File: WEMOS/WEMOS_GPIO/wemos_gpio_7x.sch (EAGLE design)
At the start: 24 parts

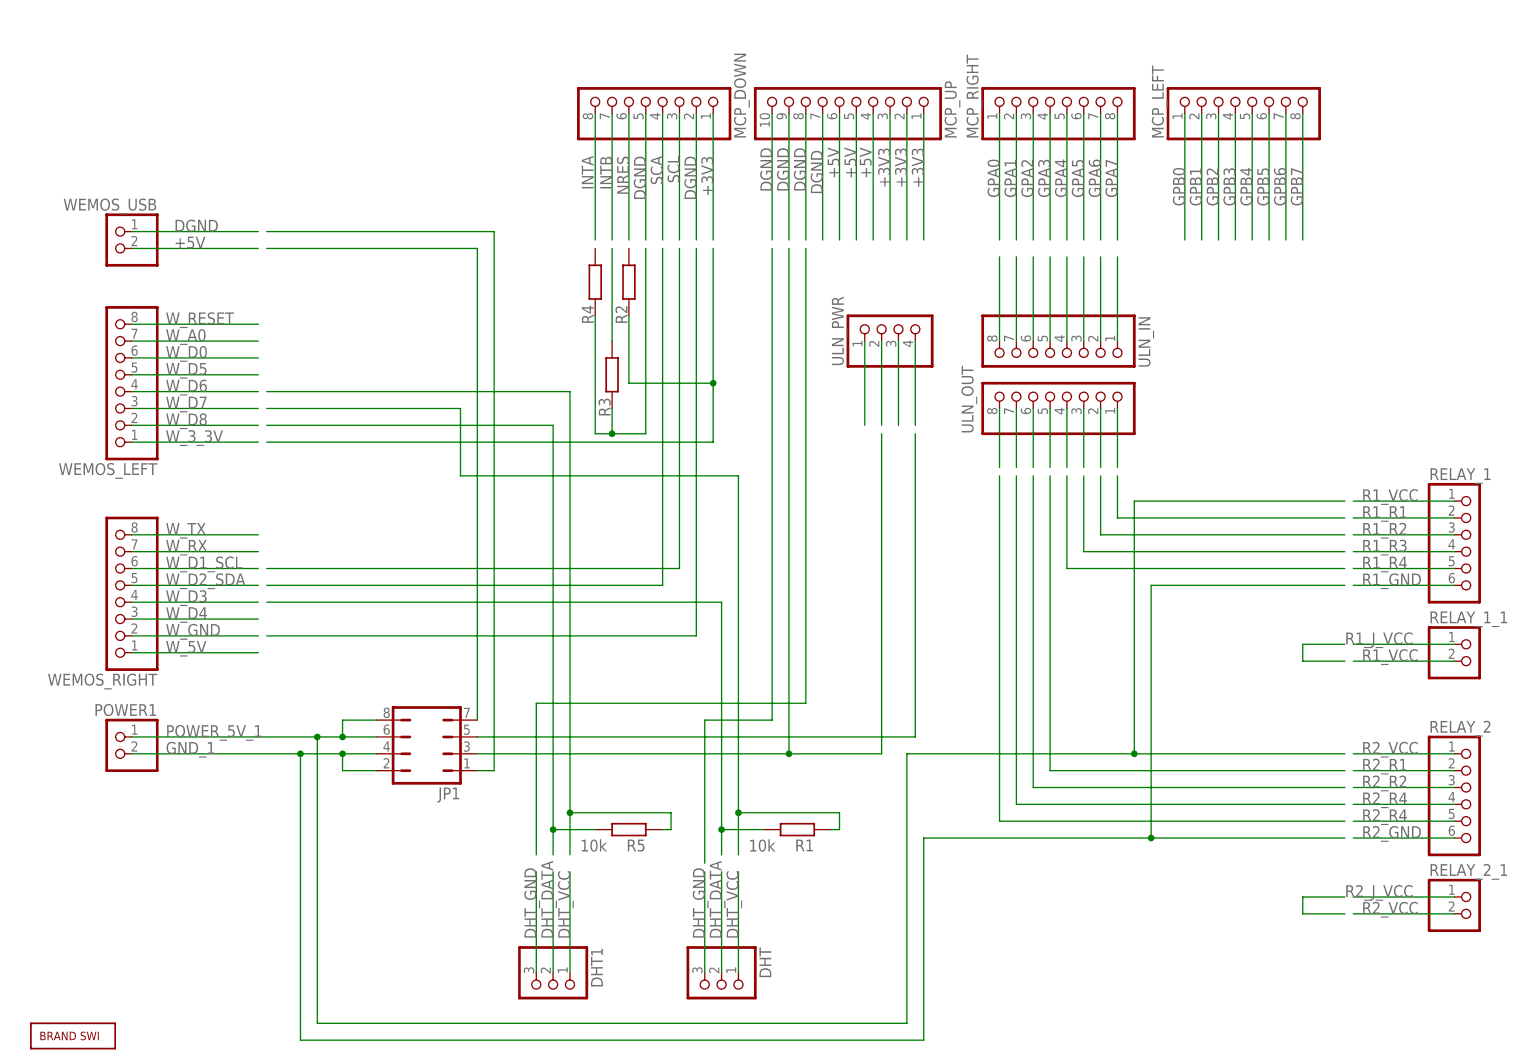
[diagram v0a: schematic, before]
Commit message: reworked wemos gpio, reworked wiring for garden control
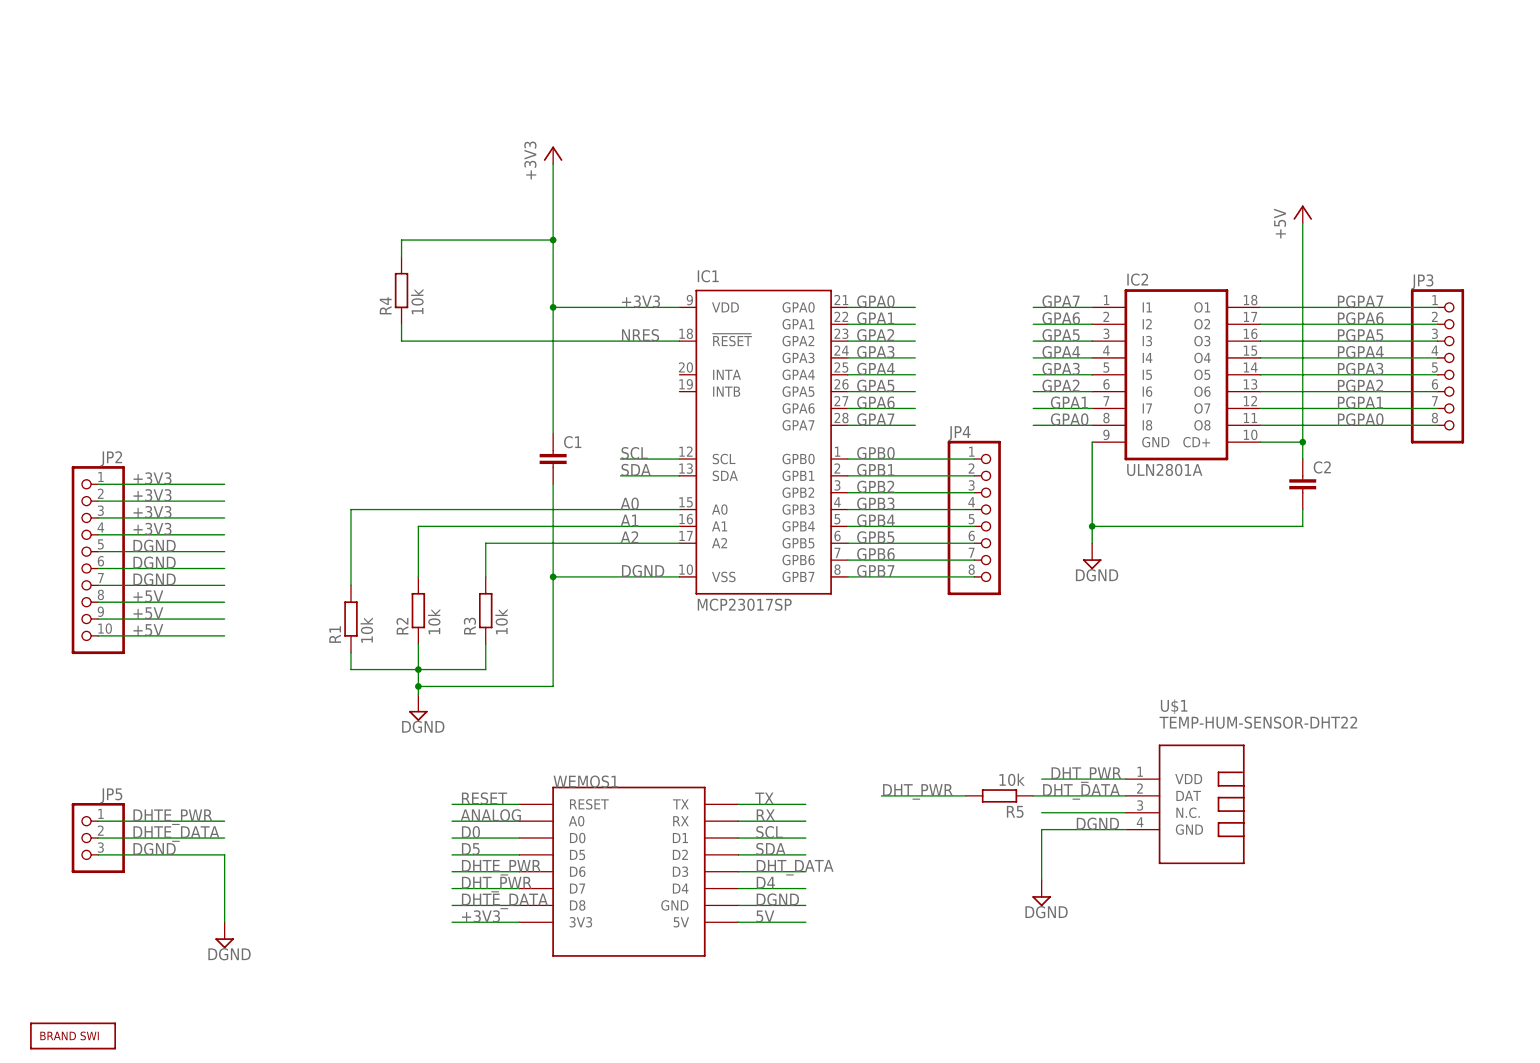
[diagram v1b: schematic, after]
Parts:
- removed DHT, DHT1: (no value), pinhead:PINHD-1X3
- removed JP1: (no value), jumper:JP4Q
- removed MCP_DOWN, MCP_LEFT, MCP_RIGHT, ULN_IN, ULN_OUT, WEMOS_LEFT, WEMOS_RIGHT: (no value), pinhead:PINHD-1X8
- removed MCP_UP: (no value), pinhead:PINHD-1X10
- removed POWER1, RELAY_1_1, RELAY_2_1, WEMOS_USB: (no value), pinhead:PINHD-1X2
- removed RELAY_1, RELAY_2: (no value), pinhead:PINHD-1X6
- removed ULN_PWR: (no value), pinhead:PINHD-1X4
- added C1, C2: (no value), rcl:C-EUC1210
- added IC1: MCP23017SP, SWI_COMMONS:MCP23017SP
- added IC2: ULN2801A, uln-udn:ULN2801A
- added JP2: (no value), pinhead:PINHD-1X10
- added JP3, JP4: (no value), pinhead:PINHD-1X8
- added JP5: (no value), pinhead:PINHD-1X3
- added U$1: TEMP-HUM-SENSOR-DHT22, SWI_COMMONS:TEMP-HUM-SENSOR-DHT22
- added WEMOS1: (no value), SWI_COMMONS:WEMOS-D1-MINI
- R1, R5: device rcl:R-EU_0207/10 -> rcl@1:R-EU_M1206
- R2, R3, R4: value (none) -> 10k; device rcl:R-EU_0204/7 -> rcl@1:R-EU_M1206
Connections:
- removed net DHT_GND: DHT.3, DHT1.3
- removed net DHT_VCC: DHT.1, DHT1.1
- removed net GND_1: JP1.2, JP1.4, POWER1.2
- removed net INTA: MCP_DOWN.8
- removed net INTB: MCP_DOWN.7
- removed net N$1: R2.1
- removed net N$11: JP1.5
- removed net N$12: JP1.1
- removed net N$13: ULN_OUT.1
- removed net N$14: ULN_OUT.2
- removed net N$15: ULN_OUT.3
- removed net N$16: ULN_OUT.4
- removed net N$17: ULN_OUT.5
- removed net N$18: ULN_OUT.6
- removed net N$19: ULN_OUT.7
- removed net N$20: ULN_OUT.8
- removed net N$21: R5.2
- removed net N$23: ULN_IN.1
- removed net N$24: ULN_IN.2
- removed net N$25: ULN_IN.3
- removed net N$26: ULN_IN.4
- removed net N$27: ULN_IN.5
- removed net N$28: ULN_IN.6
- removed net N$29: ULN_IN.7
- removed net N$30: ULN_IN.8
- removed net N$31: R5.1
- removed net N$32: R3.1, R4.1
- removed net N$33: R3.2
- removed net N$4: R1.2
- removed net N$49: ULN_PWR.1
- removed net N$5: R1.1
- removed net N$50: ULN_PWR.2
- removed net N$51: ULN_PWR.3
- removed net N$52: ULN_PWR.4
- removed net N$8: JP1.7
- removed net N$9: JP1.3
- removed net POWER_5V_1: JP1.6, JP1.8, POWER1.1
- removed net R1_GND: RELAY_1.6
- removed net R1_J_VCC: RELAY_1_1.1
- removed net R1_R1: RELAY_1.2
- removed net R1_R2: RELAY_1.3
- removed net R1_R3: RELAY_1.4
- removed net R1_R4: RELAY_1.5
- removed net R1_VCC: RELAY_1.1, RELAY_1_1.2
- removed net R2_GND: RELAY_2.6
- removed net R2_J_VCC: RELAY_2_1.1
- removed net R2_R1: RELAY_2.2
- removed net R2_R2: RELAY_2.3
- removed net R2_R4: RELAY_2.4, RELAY_2.5
- removed net R2_VCC: RELAY_2.1, RELAY_2_1.2
- removed net SCA: MCP_DOWN.4
- removed net W_3_3V: WEMOS_LEFT.1
- removed net W_5V: WEMOS_RIGHT.1
- removed net W_A0: WEMOS_LEFT.7
- removed net W_D0: WEMOS_LEFT.6
- removed net W_D1_SCL: WEMOS_RIGHT.6
- removed net W_D2_SDA: WEMOS_RIGHT.5
- removed net W_D3: WEMOS_RIGHT.4
- removed net W_D4: WEMOS_RIGHT.3
- removed net W_D5: WEMOS_LEFT.5
- removed net W_D6: WEMOS_LEFT.4
- removed net W_D7: WEMOS_LEFT.3
- removed net W_D8: WEMOS_LEFT.2
- removed net W_GND: WEMOS_RIGHT.2
- removed net W_RESET: WEMOS_LEFT.8
- removed net W_RX: WEMOS_RIGHT.7
- removed net W_TX: WEMOS_RIGHT.8
- new net 5V: WEMOS1.5V
- new net A0: IC1.A0, R1.2
- new net A1: IC1.A1, R2.2
- new net A2: IC1.A2, R3.2
- new net ANALOG: WEMOS1.A0
- new net D0: WEMOS1.D0
- new net D4: WEMOS1.D4
- new net D5: WEMOS1.D5
- new net DHTE_DATA: JP5.2, WEMOS1.D8
- new net DHTE_PWR: JP5.1, WEMOS1.D6
- new net DHT_PWR: R5.2, U$1.VDD, WEMOS1.D7
- new net N$3: U$1.N.C.
- new net PGPA0: IC2.O8, JP3.8
- new net PGPA1: IC2.O7, JP3.7
- new net PGPA2: IC2.O6, JP3.6
- new net PGPA3: IC2.O5, JP3.5
- new net PGPA4: IC2.O4, JP3.4
- new net PGPA5: IC2.O3, JP3.3
- new net PGPA6: IC2.O2, JP3.2
- new net PGPA7: IC2.O1, JP3.1
- new net RESET: WEMOS1.RESET
- new net RX: WEMOS1.RX
- new net SDA: IC1.SDA, WEMOS1.D2
- net +3V3: now also C1.1, IC1.VDD, JP2.1, JP2.2, JP2.3, JP2.4, R4.2, WEMOS1.3V3; no longer MCP_DOWN.1, MCP_UP.1, MCP_UP.2, MCP_UP.3
- net +5V: now also C2.1, IC2.CD+, JP2.10, JP2.8, JP2.9; no longer MCP_UP.5, MCP_UP.6, WEMOS_USB.2
- net DGND: now also C1.2, C2.2, IC1.VSS, IC2.GND, JP2.5, JP2.6, JP2.7, JP5.3, R1.1, R2.1, R3.1, U$1.GND, WEMOS1.GND; no longer MCP_DOWN.2, MCP_DOWN.5, MCP_UP.10, MCP_UP.8, MCP_UP.9, WEMOS_USB.1
- net DHT_DATA: now also R5.1, U$1.DAT, WEMOS1.D3; no longer DHT.2, DHT1.2
- net GPA0: now also IC1.GPA0, IC2.I8; no longer MCP_RIGHT.1
- net GPA1: now also IC1.GPA1, IC2.I7; no longer MCP_RIGHT.2
- net GPA2: now also IC1.GPA2, IC2.I6; no longer MCP_RIGHT.3
- net GPA3: now also IC1.GPA3, IC2.I5; no longer MCP_RIGHT.4
- net GPA4: now also IC1.GPA4, IC2.I4; no longer MCP_RIGHT.5
- net GPA5: now also IC1.GPA5, IC2.I3; no longer MCP_RIGHT.6
- net GPA6: now also IC1.GPA6, IC2.I2; no longer MCP_RIGHT.7
- net GPA7: now also IC1.GPA7, IC2.I1; no longer MCP_RIGHT.8
- net GPB0: now also IC1.GPB0, JP4.1; no longer MCP_LEFT.1
- net GPB1: now also IC1.GPB1, JP4.2; no longer MCP_LEFT.2
- net GPB2: now also IC1.GPB2, JP4.3; no longer MCP_LEFT.3
- net GPB3: now also IC1.GPB3, JP4.4; no longer MCP_LEFT.4
- net GPB4: now also IC1.GPB4, JP4.5; no longer MCP_LEFT.5
- net GPB5: now also IC1.GPB5, JP4.6; no longer MCP_LEFT.6
- net GPB6: now also IC1.GPB6, JP4.7; no longer MCP_LEFT.7
- net GPB7: now also IC1.GPB7, JP4.8; no longer MCP_LEFT.8
- net NRES: now also IC1.!RESET, R4.1; no longer MCP_DOWN.6
- net SCL: now also IC1.SCL, WEMOS1.D1; no longer MCP_DOWN.3
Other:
- moved on the sheet: R1, R2, R3, R4, R5

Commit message: reworked structure
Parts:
- added C3, C4: (no value), rcl@1:CPOL-EUTT5D7
- added C5, C6: (no value), rcl:C-EUC1210
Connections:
- net +3V3: now also C3.+, C5.1
- net +5V: now also C4.+, C6.1
- net DGND: now also C3.-, C4.-, C5.2, C6.2
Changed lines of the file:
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@@
 <setting verticaltext="up"/>
 </settings>
-<grid distance="0.1" unitdist="inch" unit="inch" style="lines" multiple="1" display="no" altdistance="0.01" altunitdist="inch" altunit="inch"/>
+<grid distance="50" unitdist="mil" unit="mil" style="lines" multiple="1" display="no" altdistance="0.01" altunitdist="inch" altunit="inch"/>
 <layers>
 <layer number="1" name="Top" color="4" fill="1" visible="no" active="no"/>
@@
 <part name="JP5" library="pinhead" deviceset="PINHD-1X3" device=""/>
 <part name="SUPPLY3" library="supply2" deviceset="DGND" device=""/>
+<part name="C3" library="rcl@1" deviceset="CPOL-EU" device="TT5D7"/>
+<part name="C4" library="rcl@1" deviceset="CPOL-EU" device="TT5D7"/>
+<part name="C5" library="rcl" deviceset="C-EU" device="C1210"/>
+<part name="C6" library="rcl" deviceset="C-EU" device="C1210"/>
+<part name="+3V1" library="supply1" deviceset="+3V3" device=""/>
+<part name="P+2" library="supply1@1" deviceset="+5V" device=""/>
+<part name="SUPPLY4" library="supply2" deviceset="DGND" device=""/>
+<part name="SUPPLY6" library="supply2" deviceset="DGND" device=""/>
 </parts>
 <sheets>
@@
 <instance part="JP5" gate="A" x="-91.44" y="157.48" rot="MR0"/>
 <instance part="SUPPLY3" gate="G$1" x="-69.85" y="142.24"/>
+<instance part="C3" gate="G$1" x="-96.52" y="266.7"/>
+<instance part="C4" gate="G$1" x="-71.12" y="266.7"/>
+<instance part="C5" gate="G$1" x="-88.9" y="266.7"/>
+<instance part="C6" gate="G$1" x="-63.5" y="266.7"/>
+<instance part="+3V1" gate="G$1" x="-96.52" y="279.4"/>
+<instance part="P+2" gate="1" x="-71.12" y="278.13"/>
+<instance part="SUPPLY4" gate="G$1" x="-96.52" y="252.73"/>
+<instance part="SUPPLY6" gate="G$1" x="-71.12" y="252.73"/>
 </instances>
 <busses>
@@
 <wire x1="-25.4" y1="144.78" x2="-35.56" y2="144.78" width="0.1524" layer="91"/>
 <label x="-34.29" y="144.78" size="1.778" layer="95"/>
+</segment>
+<segment>
+<pinref part="+3V1" gate="G$1" pin="+3V3"/>
+<pinref part="C3" gate="G$1" pin="+"/>
+<wire x1="-96.52" y1="276.86" x2="-96.52" y2="274.32" width="0.1524" layer="91"/>
+<pinref part="C5" gate="G$1" pin="1"/>
+<wire x1="-96.52" y1="274.32" x2="-96.52" y2="269.24" width="0.1524" layer="91"/>
+<wire x1="-96.52" y1="274.32" x2="-88.9" y2="274.32" width="0.1524" layer="91"/>
+<wire x1="-88.9" y1="274.32" x2="-88.9" y2="269.24" width="0.1524" layer="91"/>
+<junction x="-96.52" y="274.32"/>
 </segment>
 </net>
@@
 <label x="-83.82" y="200.66" size="1.778" layer="95"/>
 </segment>
+<segment>
+<pinref part="C3" gate="G$1" pin="-"/>
+<pinref part="SUPPLY4" gate="G$1" pin="DGND"/>
+<wire x1="-96.52" y1="261.62" x2="-96.52" y2="257.81" width="0.1524" layer="91"/>
+<pinref part="C5" gate="G$1" pin="2"/>
+<wire x1="-96.52" y1="257.81" x2="-96.52" y2="255.27" width="0.1524" layer="91"/>
+<wire x1="-88.9" y1="261.62" x2="-88.9" y2="257.81" width="0.1524" layer="91"/>
+<wire x1="-88.9" y1="257.81" x2="-96.52" y2="257.81" width="0.1524" layer="91"/>
+<junction x="-96.52" y="257.81"/>
+</segment>
+<segment>
+<pinref part="C4" gate="G$1" pin="-"/>
+<pinref part="SUPPLY6" gate="G$1" pin="DGND"/>
+<wire x1="-71.12" y1="261.62" x2="-71.12" y2="256.54" width="0.1524" layer="91"/>
+<pinref part="C6" gate="G$1" pin="2"/>
+<wire x1="-71.12" y1="256.54" x2="-71.12" y2="255.27" width="0.1524" layer="91"/>
+<wire x1="-63.5" y1="261.62" x2="-63.5" y2="256.54" width="0.1524" layer="91"/>
+<wire x1="-63.5" y1="256.54" x2="-71.12" y2="256.54" width="0.1524" layer="91"/>
+<junction x="-71.12" y="256.54"/>
+</segment>
 </net>
 <net name="GPB0" class="0">
@@
 <label x="-83.82" y="193.04" size="1.778" layer="95"/>
 </segment>
-</net>
+<segment>
+<pinref part="P+2" gate="1" pin="+5V"/>
+<pinref part="C4" gate="G$1" pin="+"/>
+<wire x1="-71.12" y1="275.59" x2="-71.12" y2="273.05" width="0.1524" layer="91"/>
+<pinref part="C6" gate="G$1" pin="1"/>
+<wire x1="-71.12" y1="273.05" x2="-71.12" y2="269.24" width="0.1524" layer="91"/>
+<wire x1="-71.12" y1="273.05" x2="-63.5" y2="273.05" width="0.1524" layer="91"/>
+<wire x1="-63.5" y1="273.05" x2="-63.5" y2="269.24" width="0.1524" layer="91"/>
+<junction x="-71.12" y="273.05"/>
+</segment>
+</net>
